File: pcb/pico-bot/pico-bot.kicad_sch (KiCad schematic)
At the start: 58 parts

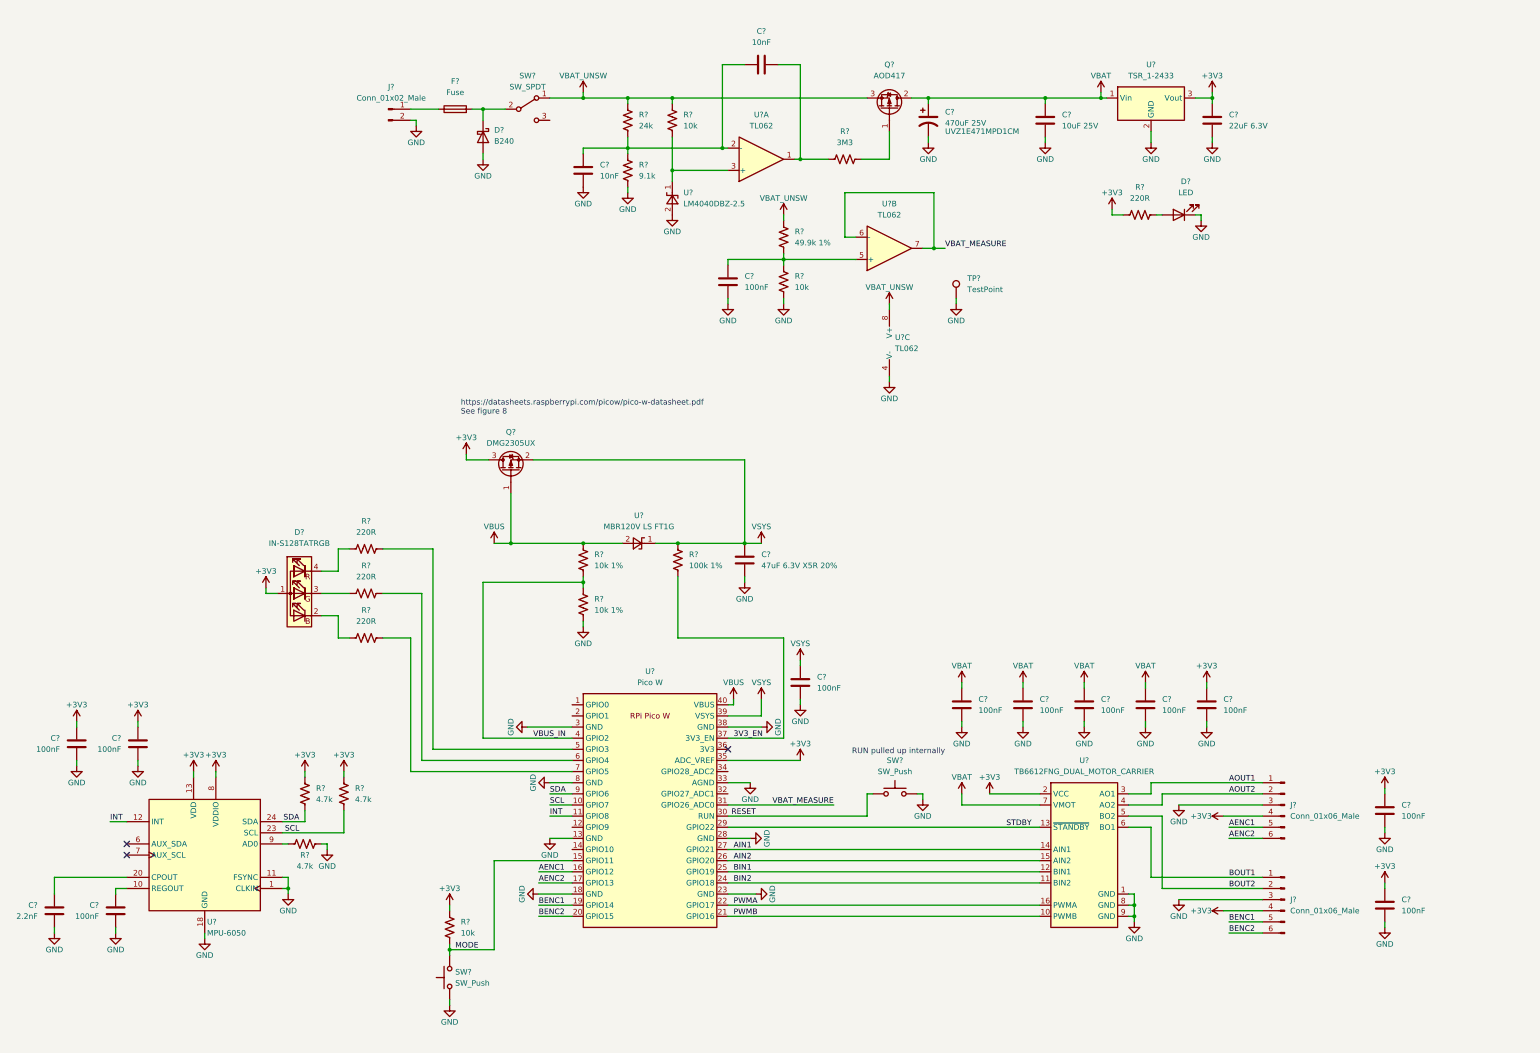
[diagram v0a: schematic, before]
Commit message: Add annotations to schematic
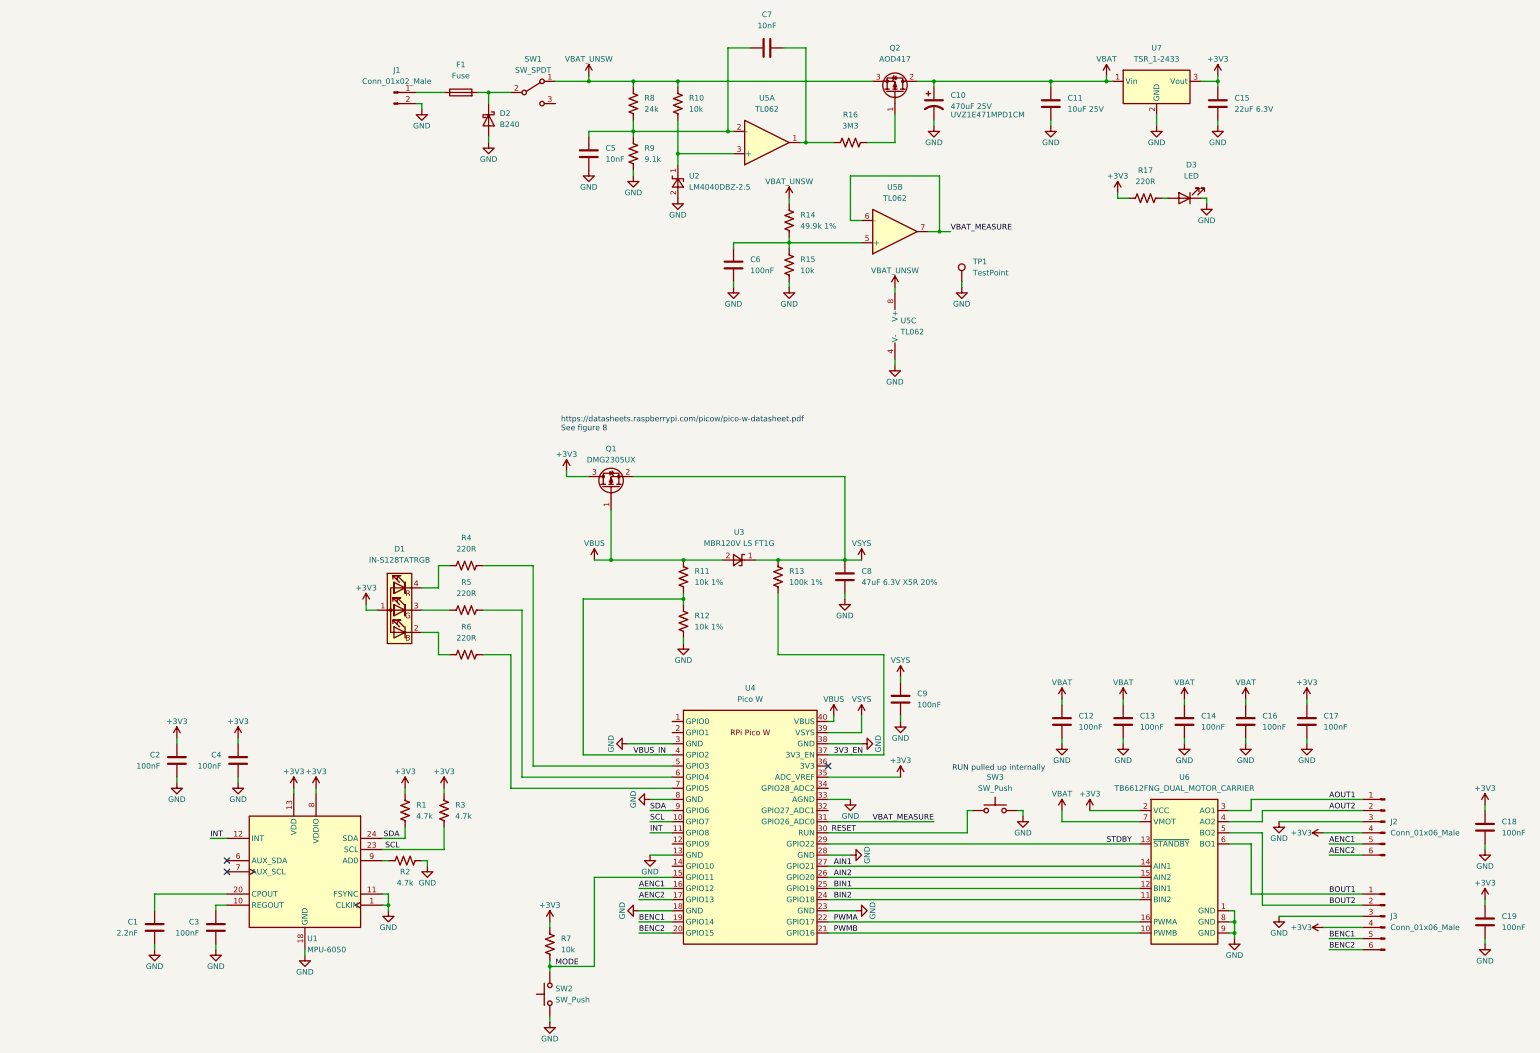
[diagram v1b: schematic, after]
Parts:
- gave numbers to parts that had none: 56
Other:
- title: (none) -> Pico-Bot
- moved on the sheet: C1, C10, C11, C12, C13, C14, C15, C16, C17, C18, C19, C2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

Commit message: Add ERC fixes, route unused GPIO and pwr/gnd to pins
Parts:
- added J4: Conn_01x06_Male, Connector_PinHeader_2.54mm:PinHeader_1x06_P2.54mm_Vertical, symbol Connector:Conn_01x06_Male
- added J5: Conn_01x04_Male, symbol Connector:Conn_01x04_Male
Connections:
- net +3V3: now also J5.1 (Pin_1), J5.2 (Pin_2)
- net GND: now also J5.3 (Pin_3), J5.4 (Pin_4)
- net GPIO0: now reaches U4.1 (GPIO0)
- net GPIO0: now also J4.1 (Pin_1)
- net GPIO9: now reaches U4.12 (GPIO9)
- net GPIO9: now also J4.3 (Pin_3)
- net GPIO10: now reaches U4.14 (GPIO10)
- net GPIO10: now also J4.4 (Pin_4)
- net GPIO1: now reaches U4.2 (GPIO1)
- net GPIO1: now also J4.2 (Pin_2)
- net GPIO27: now reaches U4.32 (GPIO27_ADC1)
- net GPIO27: now also J4.5 (Pin_5)
- net GPIO28: now reaches U4.34 (GPIO28_ADC2)
- net GPIO28: now also J4.6 (Pin_6)
- no-connect marks 3 -> 4
